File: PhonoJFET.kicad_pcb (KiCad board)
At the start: 2 copper layers, 70.1 x 54.9 mm, 38 parts, among them J1 Conn_01x02, J2 Conn_01x03, J3 Barrel_Jack_Switch, J4 Conn_01x02, J5 Conn_01x03, J6 Conn_01x01, J7 Conn_01x01, J8 Conn_01x01, J9 Conn_01x01, U1 TL072

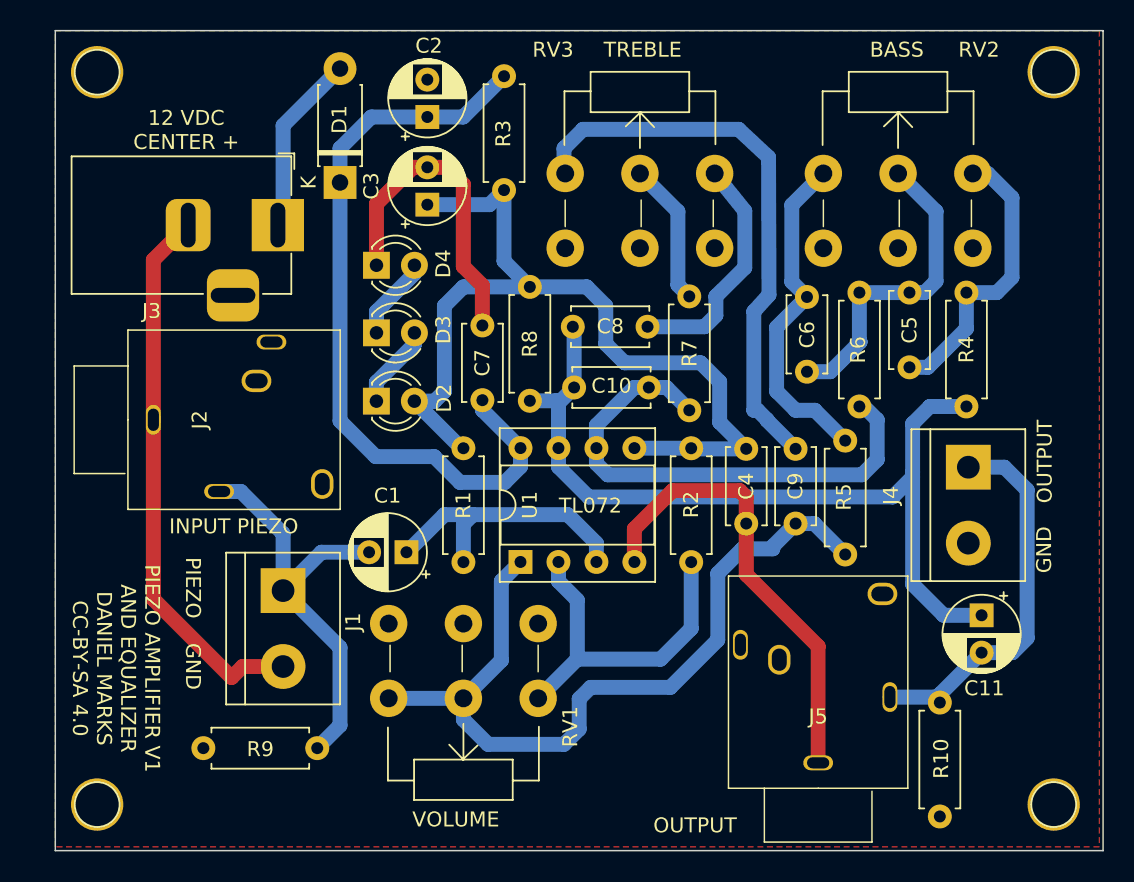
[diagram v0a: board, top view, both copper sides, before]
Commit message: Fixed some component values and biases
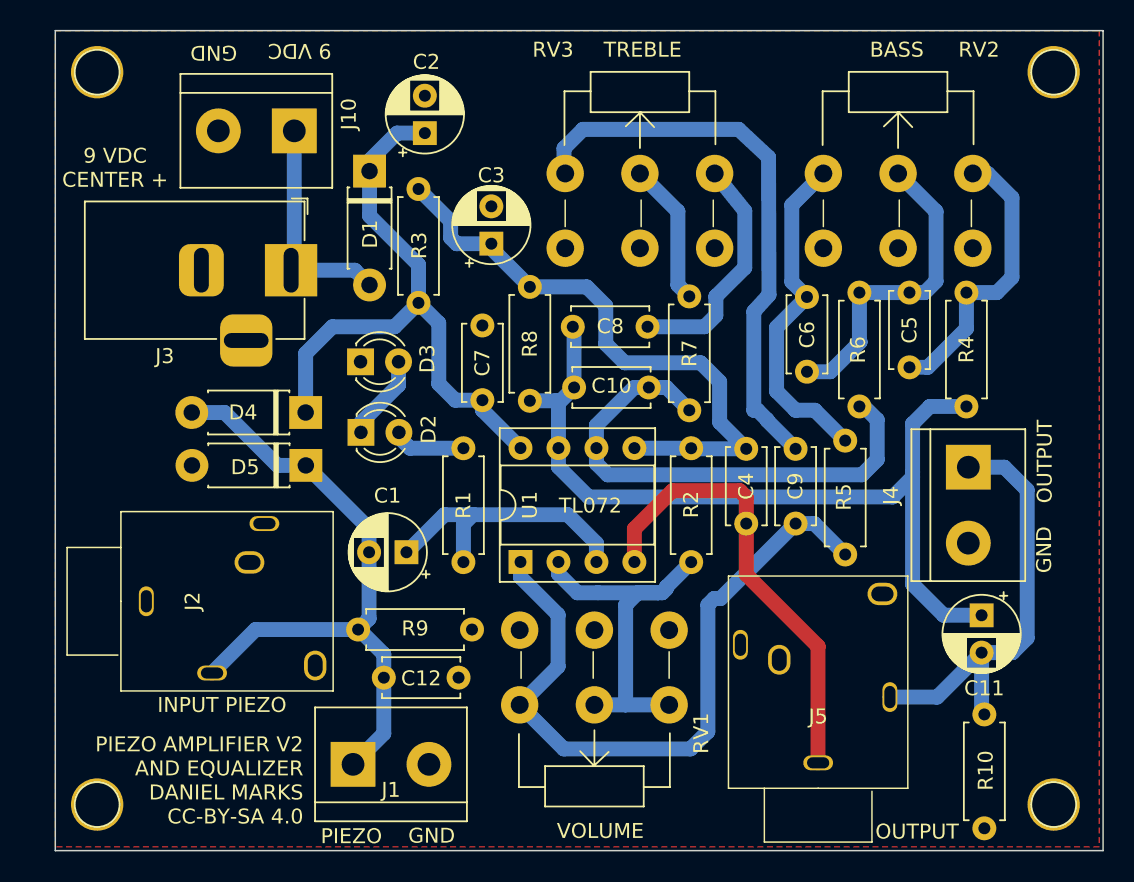
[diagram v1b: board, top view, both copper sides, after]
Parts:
- added C12: 100 pF, Capacitor_THT:C_Disc_D5.0mm_W2.5mm_P5.00mm, F.Cu at (98.2, 152.5)
- added D5: 1N4148, Diode_THT:D_DO-41_SOD81_P7.62mm_Horizontal, F.Cu at (93.0, 138.3)
- added J10: Conn_01x02, TerminalBlock:TerminalBlock_bornier-2_P5.08mm, F.Cu at (92.2, 115.9)
- D4: value LED -> 1N4148; footprint LED_THT:LED_D3.0mm -> Diode_THT:D_DO-41_SOD81_P7.62mm_Horizontal
- R10: value 100k -> 1k
- R2: value 100R -> 1k
- R3: value 330R -> 1k
- R9: value 1M -> NC
- RV1: value 10k -> 100k
- moved R3 16.2 mm to (100.5, 127.4), turned to 90 degrees
- moved J1 12.5 mm to (96.1, 158.3), turned to 0 degrees
- moved J2 12.2 mm to (80.6, 147.4)
- moved D4 10.9 mm to (93.0, 134.8), turned to 180 degrees
- moved RV1 8.78 mm to (117.3, 154.3)
- moved R9 8.39 mm to (96.5, 149.3), turned to 0 degrees
- moved C3 5.02 mm to (105.4, 123.5)
- moved J3 3.14 mm to (92.0, 125.2)
- moved R10 3.08 mm to (138.4, 162.6)
- moved D2 2.33 mm to (96.7, 136.1)
- moved D3 2.21 mm to (96.6, 131.4)
- moved D1 2.12 mm to (97.2, 118.6), turned to -90 degrees
- moved C2 1.09 mm to (100.9, 116.1)
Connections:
- C1 pad 2: Net-(J1-Pad1) -> Net-(C1-Pad2)
- D3 pad 1: Net-(D3-Pad1) -> GND
- D4 pad 1: GND -> Net-(C2-Pad1)
- D4 pad 2: Net-(D3-Pad1) -> Net-(C1-Pad2)
- J1 pad 1: Net-(J1-Pad1) -> Net-(C1-Pad2)
- J2 pad 1: Net-(J1-Pad1) -> Net-(C1-Pad2)
- R9 pad 1: Net-(J1-Pad1) -> Net-(C1-Pad2)
- RV1 pad 2: Net-(C9-Pad1) -> Net-(R2-Pad2)
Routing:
- net GND: track 89.2 -> 30.7 mm
- net Net-(C1-Pad2): track 0.00 -> 43.7 mm
- net Net-(J1-Pad1): track 29.6 -> 0.00 mm
- net +6V: track 61.1 -> 45.5 mm
- net Net-(C2-Pad1): track 50.9 -> 41.8 mm
- net Net-(C9-Pad1): track 54.2 -> 46.7 mm
- net Net-(D3-Pad1): track 5.57 -> 0.00 mm
- net +12V: track 10.5 -> 15.1 mm
- net Net-(C11-Pad2): track 25.9 -> 29.5 mm
- net Net-(R2-Pad2): track 23.6 -> 25.3 mm
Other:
- board text added: "9 VDC"
- board text added: "9 VDC CENTER +"
- board text added: "PIEZO AMPLIFIER V2 AND EQUALIZER DANIEL MARKS CC-BY-SA 4.0"
- board text removed: "12 VDC CENTER +"
- board text removed: "PIEZO AMPLIFIER V1 AND EQUALIZER DANIEL MARKS CC-BY-SA 4.0"

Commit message: Modified pcb
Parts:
- added R11: 100R, Resistor_THT:R_Axial_DIN0207_L6.3mm_D2.5mm_P7.62mm_Horizontal, F.Cu at (135.6, 153.9)
- R2: value 1k -> 100R
- RV1: value 100k -> 10k
- moved C11 2.50 mm to (135.9, 149.4), turned to 0 degrees
- moved R10 1.10 mm to (138.7, 161.5)
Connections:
- J4 pad 1: Net-(C11-Pad2) -> Net-(J4-Pad1)
- J5 pad 1: Net-(C11-Pad2) -> Net-(J4-Pad1)
- R10 pad 2: Net-(C11-Pad2) -> Net-(J4-Pad1)
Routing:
- net Net-(J4-Pad1): track 0.00 -> 37.9 mm
- net Net-(C11-Pad2): track 29.5 -> 5.71 mm
- net Net-(C10-Pad1): track 57.2 -> 55.8 mm
